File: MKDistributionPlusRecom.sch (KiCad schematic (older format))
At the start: 6 parts, among them U1 LM7805CT

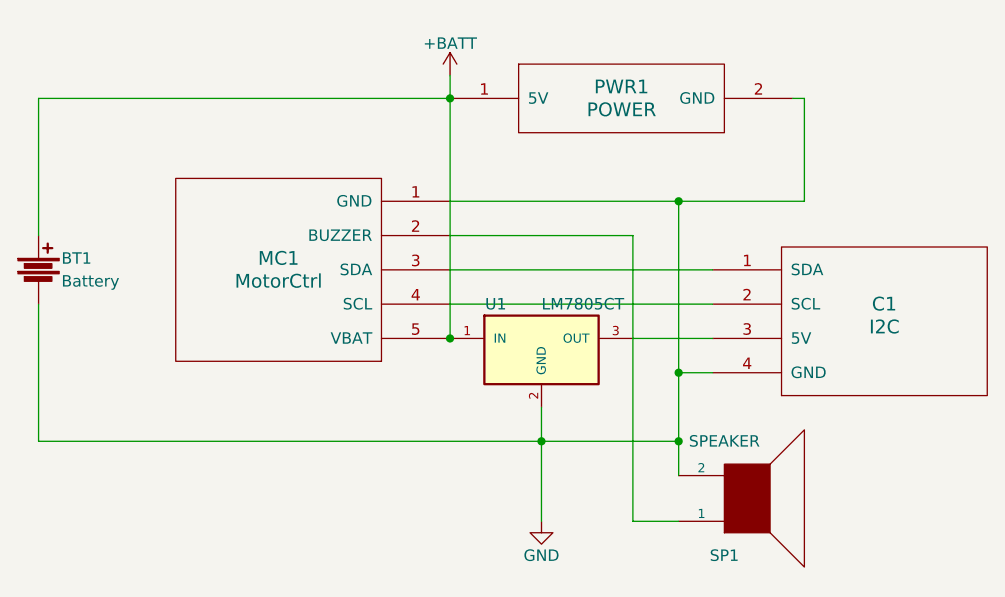
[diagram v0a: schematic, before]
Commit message: Added a second 5-pin Molex connector for BLCtrl
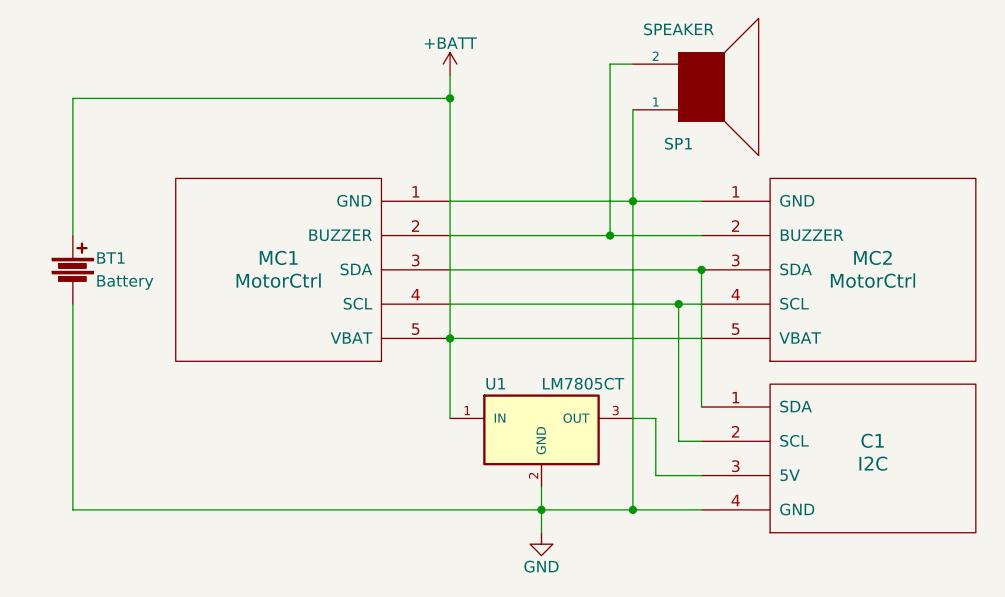
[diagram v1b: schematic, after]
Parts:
- removed PWR1: POWER, Pin_Headers:Pin_Header_Straight_1x02, symbol POWER
- added MC2: MotorCtrl, Connectors_Molex:Molex_PicoBlade_53047-0510_05x1.25mm_Straight, symbol MotorCtrl
- C1: footprint Connectors_Molex:Molex_PicoBlade_53047-0410 -> Connectors_Molex:Molex_PicoBlade_53047-0410_04x1.25mm_Straight
- MC1: footprint Connectors_Molex:Molex_PicoBlade_53047-0510 -> Connectors_Molex:Molex_PicoBlade_53047-0510_05x1.25mm_Straight
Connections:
- net +BATT: now also MC2.5 (VBAT)
- net GND: now also SP1.1, MC2.1 (GND); no longer SP1.2
- net at MC1.2 (BUZZER): now also SP1.2, MC2.2 (BUZZER); no longer SP1.1
- net at C1.1 (SDA), MC1.3 (SDA): now also MC2.3 (SDA)
- net at C1.2 (SCL), MC1.4 (SCL): now also MC2.4 (SCL)
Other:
- moved on the sheet: BT1, C1, SP1, U1
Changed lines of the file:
@@
 LIBS:mikrokopter
 LIBS:MKDistributionPlusRecom
+LIBS:MKDistributionPlusRecom-cache
 EELAYER 25 0
 EELAYER END
@@
 L SPEAKER SP1
 U 1 1 56EFFF3F
-P 4800 4250
-F 0 "SP1" H 4700 4500 50  0000 C CNN
-F 1 "SPEAKER" H 4700 4000 50  0000 C CNN
-F 2 "Pin_Headers:Pin_Header_Straight_1x02" H 4800 4250 50  0001 C CNN
-F 3 "" H 4800 4250 50  0000 C CNN
-	1    4800 4250
+P 4600 2450
+F 0 "SP1" H 4500 2700 50  0000 C CNN
+F 1 "SPEAKER" H 4500 2200 50  0000 C CNN
+F 2 "Pin_Headers:Pin_Header_Straight_1x02" H 4600 2450 50  0001 C CNN
+F 3 "" H 4600 2450 50  0000 C CNN
+	1    4600 2450
 	1    0    0    1
 $EndComp
@@
 F 0 "MC1" H 2750 3300 60  0000 C CNN
 F 1 "MotorCtrl" H 2750 3200 60  0000 C CNN
-F 2 "Connectors_Molex:Molex_PicoBlade_53047-0510" H 2750 3350 60  0001 C CNN
+F 2 "Connectors_Molex:Molex_PicoBlade_53047-0510_05x1.25mm_Straight" H 2750 3350 60  0001 C CNN
 F 3 "" H 2750 3350 60  0000 C CNN
 	1    2750 3250
@@
 L I2C C1
 U 1 1 56F001AF
-P 5400 3450
-F 0 "C1" H 5400 3500 60  0000 C CNN
-F 1 "I2C" H 5400 3400 60  0000 C CNN
-F 2 "Connectors_Molex:Molex_PicoBlade_53047-0410" H 5400 3450 60  0001 C CNN
-F 3 "" H 5400 3450 60  0000 C CNN
-	1    5400 3450
+P 5350 4050
+F 0 "C1" H 5350 4100 60  0000 C CNN
+F 1 "I2C" H 5350 4000 60  0000 C CNN
+F 2 "Connectors_Molex:Molex_PicoBlade_53047-0410_04x1.25mm_Straight" H 5350 4050 60  0001 C CNN
+F 3 "" H 5350 4050 60  0000 C CNN
+	1    5350 4050
+	1    0    0    -1
+$EndComp
+$Comp
+L LM7805CT U1
+U 1 1 56F00BF5
+P 3900 3950
+F 0 "U1" H 3700 4150 50  0000 C CNN
+F 1 "LM7805CT" H 3900 4150 50  0000 L CNN
+F 2 "Converters_DCDC_ACDC:DCDC-Conv_Recom_R-78HBxx-0.5" H 3900 4050 50  0001 C CIN
+F 3 "" H 3900 3950 50  0000 C CNN
+	1    3900 3950
+	1    0    0    -1
+$EndComp
+$Comp
+L GND #PWR02
+U 1 1 56F15B6B
+P 3900 4400
+F 0 "#PWR02" H 3900 4150 50  0001 C CNN
+F 1 "GND" H 3900 4250 50  0000 C CNN
+F 2 "" H 3900 4400 50  0000 C CNN
+F 3 "" H 3900 4400 50  0000 C CNN
+	1    3900 4400
+	1    0    0    -1
+$EndComp
+$Comp
+L Battery BT1
+U 1 1 5747A1BA
+P 1850 3250
+F 0 "BT1" H 1950 3300 50  0000 L CNN
+F 1 "Battery" H 1950 3200 50  0000 L CNN
+F 2 "Pin_Headers:Pin_Header_Straight_1x02" V 1850 3290 50  0001 C CNN
+F 3 "" V 1850 3290 50  0000 C CNN
+	1    1850 3250
+	1    0    0    -1
+$EndComp
+$Comp
+L MotorCtrl MC2
+U 1 1 5841602E
+P 5350 3250
+F 0 "MC2" H 5350 3300 60  0000 C CNN
+F 1 "MotorCtrl" H 5350 3200 60  0000 C CNN
+F 2 "Connectors_Molex:Molex_PicoBlade_53047-0510_05x1.25mm_Straight" H 5350 3350 60  0001 C CNN
+F 3 "" H 5350 3350 60  0000 C CNN
+	1    5350 3250
 	1    0    0    -1
 $EndComp
 Wire Wire Line
-	3500 3250 4650 3250
+	3500 3250 4600 3250
 Wire Wire Line
-	3500 3400 4650 3400
+	3500 3400 4600 3400
 Wire Wire Line
-	3500 2950 5050 2950
+	3900 4200 3900 4400
+Connection ~ 4300 4300
 Wire Wire Line
-	4500 3700 4650 3700
-Connection ~ 4500 3700
+	3500 2400 3500 3900
+Connection ~ 4300 2950
+Connection ~ 3500 2500
 Wire Wire Line
-	3500 3100 4300 3100
+	5000 2500 5000 2500
+Connection ~ 3900 4300
 Wire Wire Line
-	4300 3100 4300 4350
+	1850 2500 1850 3100
 Wire Wire Line
-	4300 4350 4500 4350
+	1850 4300 1850 3400
+Connection ~ 4200 3100
 Wire Wire Line
-	4300 3550 4650 3550
+	4300 4300 4300 2550
+Connection ~ 4500 3400
+Connection ~ 4600 3250
 Wire Wire Line
-	3900 3850 3900 4350
+	4200 2350 4300 2350
 Wire Wire Line
-	1700 4000 4500 4000
-Connection ~ 4500 4000
+	4200 3100 4200 2350
+Wire Wire Line
+	1850 4300 4600 4300
+Wire Wire Line
+	4600 4150 4400 4150
+Wire Wire Line
+	4600 4000 4500 4000
+Wire Wire Line
+	4500 4000 4500 3400
+Wire Wire Line
+	4600 3250 4600 3850
+Wire Wire Line
+	3500 2950 4600 2950
+Wire Wire Line
+	3500 3100 4600 3100
+Wire Wire Line
+	1850 2500 3500 2500
+Wire Wire Line
+	4400 4150 4400 3900
+Wire Wire Line
+	4400 3900 4300 3900
 Connection ~ 3500 3550
 Wire Wire Line
-	3500 2400 3500 3550
-$Comp
-L LM7805CT U1
-U 1 1 56F00BF5
-P 3900 3600
-F 0 "U1" H 3700 3800 50  0000 C CNN
-F 1 "LM7805CT" H 3900 3800 50  0000 L CNN
-F 2 "Converters_DCDC_ACDC:DCDC-Conv_Recom_R-78HBxx-0.5" H 3900 3700 50  0001 C CIN
-F 3 "" H 3900 3600 50  0000 C CNN
-	1    3900 3600
-	1    0    0    -1
-$EndComp
-Connection ~ 4500 2950
-Connection ~ 3500 2500
-$Comp
-L POWER PWR1
-U 1 1 56F15ADC
-P 4250 2500
-F 0 "PWR1" H 4250 2550 60  0000 C CNN
-F 1 "POWER" H 4250 2450 60  0000 C CNN
-F 2 "Pin_Headers:Pin_Header_Straight_1x02" H 4250 2500 60  0001 C CNN
-F 3 "" H 4250 2500 60  0000 C CNN
-	1    4250 2500
-	1    0    0    -1
-$EndComp
-Wire Wire Line
-	4500 2950 4500 4150
-Wire Wire Line
-	5000 2500 5050 2500
-Wire Wire Line
-	5050 2500 5050 2950
-$Comp
-L GND #PWR02
-U 1 1 56F15B6B
-P 3900 4350
-F 0 "#PWR02" H 3900 4100 50  0001 C CNN
-F 1 "GND" H 3900 4200 50  0000 C CNN
-F 2 "" H 3900 4350 50  0000 C CNN
-F 3 "" H 3900 4350 50  0000 C CNN
-	1    3900 4350
-	1    0    0    -1
-$EndComp
-Connection ~ 3900 4000
-$Comp
-L Battery BT1
-U 1 1 5747A1BA
-P 1700 3250
-F 0 "BT1" H 1800 3300 50  0000 L CNN
-F 1 "Battery" H 1800 3200 50  0000 L CNN
-F 2 "Pin_Headers:Pin_Header_Straight_1x02" V 1700 3290 50  0001 C CNN
-F 3 "" V 1700 3290 50  0000 C CNN
-	1    1700 3250
-	1    0    0    -1
-$EndComp
-Wire Wire Line
-	3500 2500 1700 2500
-Wire Wire Line
-	1700 2500 1700 3100
-Wire Wire Line
-	1700 4000 1700 3400
+	4600 3550 3500 3550
 $EndSCHEMATC
